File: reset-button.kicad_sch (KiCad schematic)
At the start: 3 parts, among them SW1 SW_MEC_5E

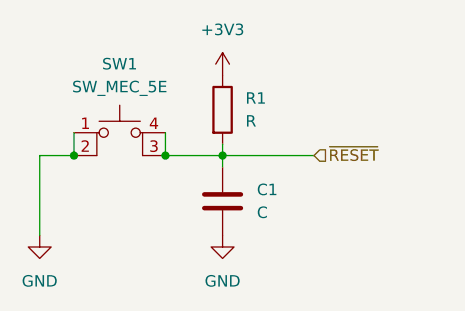
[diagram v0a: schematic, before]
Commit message: Adding symbols information
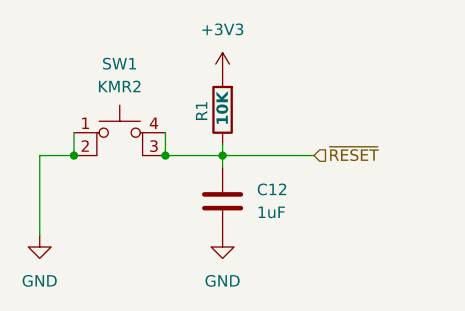
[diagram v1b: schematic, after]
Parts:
- C12: renamed from C1; value C -> 1uF; footprint (none) -> Capacitor_SMD:C_0603_1608Metric; Mfr (none) -> YAGEO; Mfr P/N (none) -> CC0603KRX7R7BB105; Supplier_1 (none) -> Digikey; Supplier_1 P/N (none) -> 0.10; Supplier_1 Unit Price (none) -> 0.03080
- R1: value R -> 10K; footprint (none) -> Resistor_SMD:R_0603_1608Metric; Mfr (none) -> Stackpole Electronics Inc; Mfr P/N (none) -> RNCP0603FTD10K0; Supplier_1 (none) -> Digikey; Supplier_1 P/N (none) -> RNCP0603FTD10K0CT-ND; Supplier_1 Price @ Qty (none) -> 0.0170; Supplier_1 Unit Price (none) -> 0.10
- SW1: value SW_MEC_5E -> KMR2; footprint (none) -> Button_Switch_SMD:SW_Push_1P1T_NO_CK_KMR2; Mfr (none) -> C&K; Mfr P/N (none) -> KM241NG ULC LFS; Supplier_1 (none) -> Digikey; Supplier_1 P/N (none) -> CKN10285CT-ND; Supplier_1 Price @ Qty (none) -> 0.72030; Supplier_1 Unit Price (none) -> 0.92
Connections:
- net +3V3: now also R1.2; no longer R1.1
- net ~{RESET}: now also R1.1; no longer R1.2
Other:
- company: (none) -> catbranchman
- title: (none) -> Reset Button

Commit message: Starting layout
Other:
- moved on the sheet: C12, R1
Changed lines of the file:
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@@
 	)
 	(junction
-		(at 153.67 97.79)
+		(at 156.21 97.79)
 		(diameter 0)
 		(color 0 0 0 0)
 	)
 	(junction
-		(at 137.16 97.79)
+		(at 135.89 97.79)
 		(diameter 0)
 		(color 0 0 0 0)
 	)
 	(junction
-		(at 147.32 97.79)
+		(at 148.59 97.79)
 		(diameter 0)
 		(color 0 0 0 0)
@@
 	(wire
 		(pts
-			(xy 153.67 97.79) (xy 153.67 99.06)
-		)
-		(stroke
-			(width 0)
-			(type default)
-		)
-	)
-	(wire
-		(pts
-			(xy 137.16 95.25) (xy 137.16 97.79)
+			(xy 156.21 97.79) (xy 156.21 99.06)
+		)
+		(stroke
+			(width 0)
+			(type default)
+		)
+	)
+	(wire
+		(pts
+			(xy 135.89 97.79) (xy 137.16 97.79)
+		)
+		(stroke
+			(width 0)
+			(type default)
+		)
+	)
+	(wire
+		(pts
+			(xy 133.35 97.79) (xy 135.89 97.79)
 		)
 		(stroke
@@
 	(wire
 		(pts
-			(xy 147.32 95.25) (xy 147.32 97.79)
-		)
-		(stroke
-			(width 0)
-			(type default)
-		)
-	)
-	(wire
-		(pts
-			(xy 147.32 97.79) (xy 153.67 97.79)
-		)
-		(stroke
-			(width 0)
-			(type default)
-		)
-	)
-	(wire
-		(pts
-			(xy 153.67 97.79) (xy 163.83 97.79)
-		)
-		(stroke
-			(width 0)
-			(type default)
-		)
-	)
-	(wire
-		(pts
-			(xy 133.35 97.79) (xy 137.16 97.79)
-		)
-		(stroke
-			(width 0)
-			(type default)
-		)
-	)
-	(wire
-		(pts
-			(xy 153.67 97.79) (xy 153.67 96.52)
+			(xy 148.59 95.25) (xy 148.59 97.79)
+		)
+		(stroke
+			(width 0)
+			(type default)
+		)
+	)
+	(wire
+		(pts
+			(xy 135.89 95.25) (xy 135.89 97.79)
+		)
+		(stroke
+			(width 0)
+			(type default)
+		)
+	)
+	(wire
+		(pts
+			(xy 156.21 97.79) (xy 166.37 97.79)
+		)
+		(stroke
+			(width 0)
+			(type default)
+		)
+	)
+	(wire
+		(pts
+			(xy 147.32 97.79) (xy 148.59 97.79)
+		)
+		(stroke
+			(width 0)
+			(type default)
+		)
+	)
+	(wire
+		(pts
+			(xy 148.59 95.25) (xy 147.32 95.25)
+		)
+		(stroke
+			(width 0)
+			(type default)
+		)
+	)
+	(wire
+		(pts
+			(xy 156.21 97.79) (xy 156.21 96.52)
+		)
+		(stroke
+			(width 0)
+			(type default)
+		)
+	)
+	(wire
+		(pts
+			(xy 148.59 97.79) (xy 156.21 97.79)
+		)
+		(stroke
+			(width 0)
+			(type default)
+		)
+	)
+	(wire
+		(pts
+			(xy 137.16 95.25) (xy 135.89 95.25)
 		)
 		(stroke
@@
 	(hierarchical_label "~{RESET}"
 		(shape input)
-		(at 163.83 97.79 0)
+		(at 166.37 97.79 0)
 		(fields_autoplaced yes)
 		(effects
@@
 	(symbol
 		(lib_id "Device:C")
-		(at 153.67 102.87 0)
+		(at 156.21 102.87 0)
 		(unit 1)
 		(exclude_from_sim no)
@@
 		(fields_autoplaced yes)
 		(property "Reference" "C12"
-			(at 157.48 101.5999 0)
+			(at 160.02 101.5999 0)
 			(effects
 				(font
@@
 		)
 		(property "Value" "1uF"
-			(at 157.48 104.1399 0)
+			(at 160.02 104.1399 0)
 			(effects
 				(font
@@
 		)
 		(property "Footprint" "Capacitor_SMD:C_0603_1608Metric"
-			(at 154.6352 106.68 0)
+			(at 157.1752 106.68 0)
 			(effects
 				(font
@@
 		)
 		(property "Datasheet" "https://www.yageo.com/upload/media/product/productsearch/datasheet/mlcc/UPY-GPHC_X7R_6"
-			(at 153.67 102.87 0)
+			(at 156.21 102.87 0)
 			(effects
 				(font
@@
 		)
 		(property "Description" "1 uF 10% 16V Ceramic Capacitor X7R 0603 (1608 Metric)"
-			(at 153.67 102.87 0)
+			(at 156.21 102.87 0)
 			(effects
 				(font
@@
 		)
 		(property "Mfr" "YAGEO"
-			(at 153.67 102.87 0)
+			(at 156.21 102.87 0)
 			(effects
 				(font
@@
 		)
 		(property "Mfr P/N" "CC0603KRX7R7BB105"
-			(at 153.67 102.87 0)
+			(at 156.21 102.87 0)
 			(effects
 				(font
@@
 		)
 		(property "Supplier_1" "Digikey"
-			(at 153.67 102.87 0)
+			(at 156.21 102.87 0)
 			(effects
 				(font
@@
 		)
 		(property "Supplier_1 P/N" "0.10"
-			(at 153.67 102.87 0)
+			(at 156.21 102.87 0)
 			(effects
 				(font
@@
 		)
 		(property "Supplier_1 Unit Price" "0.03080"
-			(at 153.67 102.87 0)
+			(at 156.21 102.87 0)
 			(effects
 				(font
@@
 		)
 		(property "Supplier_1 Price @ Qty" ""
-			(at 153.67 102.87 0)
+			(at 156.21 102.87 0)
 			(effects
 				(font
@@
 		)
 		(property "Supplier_2" ""
-			(at 153.67 102.87 0)
+			(at 156.21 102.87 0)
 			(effects
 				(font
@@
 		)
 		(property "Supplier_2 P/N" ""
-			(at 153.67 102.87 0)
+			(at 156.21 102.87 0)
 			(effects
 				(font
@@
 		)
 		(property "Supplier_2 Unit Price" ""
-			(at 153.67 102.87 0)
+			(at 156.21 102.87 0)
 			(effects
 				(font
@@
 		)
 		(property "Supplier_2 Price @ Qty" ""
-			(at 153.67 102.87 0)
+			(at 156.21 102.87 0)
 			(effects
 				(font
@@
 	(symbol
 		(lib_id "Device:R")
-		(at 153.67 92.71 180)
+		(at 156.21 92.71 180)
 		(unit 1)
 		(exclude_from_sim no)
@@
 		(dnp no)
 		(property "Reference" "R1"
-			(at 151.384 91.694 90)
+			(at 153.924 91.694 90)
 			(effects
 				(font
@@
 		)
 		(property "Value" "10K"
-			(at 153.67 90.678 90)
+			(at 156.21 90.678 90)
 			(effects
 				(font
@@
 		)
 		(property "Footprint" "Resistor_SMD:R_0603_1608Metric"
-			(at 155.448 92.71 90)
+			(at 157.988 92.71 90)
 			(effects
 				(font
@@
 		)
 		(property "Datasheet" "https://www.seielect.com/catalog/sei-rncp.pdf"
-			(at 153.67 92.71 0)
+			(at 156.21 92.71 0)
 			(effects
 				(font
@@
 		)
 		(property "Description" "10 kOhms 1% 0.125W, 1/8W Chip Resistor 0603 (1608 Metric) Anti-Sulfur Thin Film"
-			(at 153.67 92.71 0)
+			(at 156.21 92.71 0)
 			(effects
 				(font
@@
 		)
 		(property "Mfr" "Stackpole Electronics Inc"
-			(at 153.67 92.71 0)
+			(at 156.21 92.71 0)
 			(effects
 				(font
@@
 		)
 		(property "Mfr P/N" "RNCP0603FTD10K0"
-			(at 153.67 92.71 0)
+			(at 156.21 92.71 0)
 			(effects
 				(font
@@
 		)
 		(property "Supplier_1" "Digikey"
-			(at 153.67 92.71 0)
+			(at 156.21 92.71 0)
 			(effects
 				(font
@@
 		)
 		(property "Supplier_1 P/N" "RNCP0603FTD10K0CT-ND"
-			(at 153.67 92.71 0)
+			(at 156.21 92.71 0)
 			(effects
 				(font
@@
 		)
 		(property "Supplier_1 Unit Price" "0.10"
-			(at 153.67 92.71 0)
+			(at 156.21 92.71 0)
 			(effects
 				(font
@@
 		)
 		(property "Supplier_1 Price @ Qty" "0.0170"
-			(at 153.67 92.71 0)
+			(at 156.21 92.71 0)
 			(effects
 				(font
@@
 		)
 		(property "Supplier_2" ""
-			(at 153.67 92.71 0)
+			(at 156.21 92.71 0)
 			(effects
 				(font
@@
 		)
 		(property "Supplier_2 P/N" ""
-			(at 153.67 92.71 0)
+			(at 156.21 92.71 0)
 			(effects
 				(font
@@
 		)
 		(property "Supplier_2 Unit Price" ""
-			(at 153.67 92.71 0)
+			(at 156.21 92.71 0)
 			(effects
 				(font
@@
 		)
 		(property "Supplier_2 Price @ Qty" ""
-			(at 153.67 92.71 0)
+			(at 156.21 92.71 0)
 			(effects
 				(font
@@
 	(symbol
 		(lib_id "power:+3V3")
-		(at 153.67 88.9 0)
+		(at 156.21 88.9 0)
 		(unit 1)
 		(exclude_from_sim no)
@@
 		(fields_autoplaced yes)
 		(property "Reference" "#PWR03"
-			(at 153.67 92.71 0)
+			(at 156.21 92.71 0)
 			(effects
 				(font
@@
 		)
 		(property "Value" "+3V3"
-			(at 153.67 83.82 0)
+			(at 156.21 83.82 0)
 			(effects
 				(font
@@
 		)
 		(property "Footprint" ""
-			(at 153.67 88.9 0)
+			(at 156.21 88.9 0)
 			(effects
 				(font
@@
 		)
 		(property "Datasheet" ""
-			(at 153.67 88.9 0)
+			(at 156.21 88.9 0)
 			(effects
 				(font
@@
 		)
 		(property "Description" "Power symbol creates a global label with name \"+3V3\""
-			(at 153.67 88.9 0)
+			(at 156.21 88.9 0)
 			(effects
 				(font
@@
 	(symbol
 		(lib_id "power:GND")
-		(at 153.67 106.68 0)
+		(at 156.21 106.68 0)
 		(unit 1)
 		(exclude_from_sim no)
@@
 		(fields_autoplaced yes)
 		(property "Reference" "#PWR02"
-			(at 153.67 113.03 0)
+			(at 156.21 113.03 0)
 			(effects
 				(font
@@
 		)
 		(property "Value" "GND"
-			(at 153.67 111.76 0)
+			(at 156.21 111.76 0)
 			(effects
 				(font
@@
 		)
 		(property "Footprint" ""
-			(at 153.67 106.68 0)
+			(at 156.21 106.68 0)
 			(effects
 				(font
@@
 		)
 		(property "Datasheet" ""
-			(at 153.67 106.68 0)
+			(at 156.21 106.68 0)
 			(effects
 				(font
@@
 		)
 		(property "Description" "Power symbol creates a global label with name \"GND\" , ground"
-			(at 153.67 106.68 0)
-			(effects
-				(font
+			(at 156.21 106.68 0)
+			(effects
+				(font

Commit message: Working on layout
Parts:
- removed SW1: KMR2, Button_Switch_SMD:SW_Push_1P1T_NO_CK_KMR2, symbol Switch:SW_MEC_5E
- added SW1: KMR2, Button_Switch_SMD:SW_Push_1P1T_NO_CK_KMR2, symbol Switch:SW_Push
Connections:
- net GND: now also SW1.1
- net ~{RESET}: now also SW1.2
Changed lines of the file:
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@@
-		(color 0 0 0 0)
-	)
-	(junction
-		(at 135.89 97.79)
-		(diameter 0)
-		(color 0 0 0 0)
-	)
-	(junction
-		(at 148.59 97.79)
-		(diameter 0)
 		(color 0 0 0 0)
 	)
@@
 	(wire
 		(pts
-			(xy 135.89 97.79) (xy 137.16 97.79)
+			(xy 133.35 97.79) (xy 137.16 97.79)
 		)
 		(stroke
@@
 	(wire
 		(pts
-			(xy 133.35 97.79) (xy 135.89 97.79)
+			(xy 133.35 106.68) (xy 133.35 97.79)
 		)
 		(stroke
@@
 	(wire
 		(pts
-			(xy 133.35 106.68) (xy 133.35 97.79)
+			(xy 156.21 97.79) (xy 166.37 97.79)
 		)
 		(stroke
@@
 	(wire
 		(pts
-			(xy 148.59 95.25) (xy 148.59 97.79)
+			(xy 147.32 97.79) (xy 156.21 97.79)
 		)
 		(stroke
@@
 	(wire
 		(pts
-			(xy 135.89 95.25) (xy 135.89 97.79)
-		)
-		(stroke
-			(width 0)
-			(type default)
-		)
-	)
-	(wire
-		(pts
-			(xy 156.21 97.79) (xy 166.37 97.79)
-		)
-		(stroke
-			(width 0)
-			(type default)
-		)
-	)
-	(wire
-		(pts
-			(xy 147.32 97.79) (xy 148.59 97.79)
-		)
-		(stroke
-			(width 0)
-			(type default)
-		)
-	)
-	(wire
-		(pts
-			(xy 148.59 95.25) (xy 147.32 95.25)
-		)
-		(stroke
-			(width 0)
-			(type default)
-		)
-	)
-	(wire
-		(pts
 			(xy 156.21 97.79) (xy 156.21 96.52)
-		)
-		(stroke
-			(width 0)
-			(type default)
-		)
-	)
-	(wire
-		(pts
-			(xy 148.59 97.79) (xy 156.21 97.79)
-		)
-		(stroke
-			(width 0)
-			(type default)
-		)
-	)
-	(wire
-		(pts
-			(xy 137.16 95.25) (xy 135.89 95.25)
 		)
 		(stroke
@@
 	)
 	(symbol
-		(lib_id "Switch:SW_MEC_5E")
-		(at 142.24 97.79 0)
-		(unit 1)
-		(exclude_from_sim no)
-		(in_bom yes)
-		(on_board yes)
-		(dnp no)
-		(fields_autoplaced yes)
-		(property "Reference" "SW1"
-			(at 142.24 87.63 0)
-			(effects
-				(font
-					(size 1.27 1.27)
-				)
-			)
-		)
-		(property "Value" "KMR2"
-			(at 142.24 90.17 0)
-			(effects
-				(font
-					(size 1.27 1.27)
-				)
-			)
-		)
-		(property "Footprint" "Button_Switch_SMD:SW_Push_1P1T_NO_CK_KMR2"
-			(at 142.24 90.17 0)
-			(effects
-				(font
-					(size 1.27 1.27)
-				)
-				(hide yes)
-			)
-		)
-		(property "Datasheet" "https://www.ckswitches.com/media/1479/kmr2.pdf"
-			(at 142.24 90.17 0)
-			(effects
-				(font
-					(size 1.27 1.27)
-				)
-				(hide yes)
-			)
-		)
-		(property "Description" "Tactile Switch SPST-NO Top Actuated Surface Mount 0.05A @ 32 VDC 400gf"
-			(at 142.24 97.79 0)
-			(effects
-				(font
-					(size 1.27 1.27)
-				)
-				(hide yes)
-			)
-		)
-		(property "Mfr" "C&K"
-			(at 142.24 97.79 0)
-			(effects
-				(font
-					(size 1.27 1.27)
-				)
-				(hide yes)
-			)
-		)
-		(property "Mfr P/N" "KM241NG ULC LFS"
-			(at 142.24 97.79 0)
-			(effects
-				(font
-					(size 1.27 1.27)
-				)
-				(hide yes)
-			)
-		)
-		(property "Supplier_1" "Digikey"
-			(at 142.24 97.79 0)
-			(effects
-				(font
-					(size 1.27 1.27)
-				)
-				(hide yes)
-			)
-		)
-		(property "Supplier_1 P/N" "CKN10285CT-ND"
-			(at 142.24 97.79 0)
-			(effects
-				(font
-					(size 1.27 1.27)
-				)
-				(hide yes)
-			)
-		)
-		(property "Supplier_1 Unit Price" "0.92"
-			(at 142.24 97.79 0)
-			(effects
-				(font
-					(size 1.27 1.27)
-				)
-				(hide yes)
-			)
-		)
-		(property "Supplier_1 Price @ Qty" "0.72030"
-			(at 142.24 97.79 0)
-			(effects
-				(font
-					(size 1.27 1.27)
-				)
-				(hide yes)
-			)
-		)
-		(property "Supplier_2" ""
-			(at 142.24 97.79 0)
-			(effects
-				(font
-					(size 1.27 1.27)
-				)
-				(hide yes)
-			)
-		)
-		(property "Supplier_2 P/N" ""
-			(at 142.24 97.79 0)
-			(effects
-				(font
-					(size 1.27 1.27)
-				)
-				(hide yes)
-			)
-		)
-		(property "Supplier_2 Unit Price" ""
-			(at 142.24 97.79 0)
-			(effects
-				(font
-					(size 1.27 1.27)
-				)
-				(hide yes)
-			)
-		)
-		(property "Supplier_2 Price @ Qty" ""
-			(at 142.24 97.79 0)
-			(effects
-				(font
-					(size 1.27 1.27)
-				)
-				(hide yes)
-			)
-		)
-		(pin "2"
-		)
-		(pin "3"
-		)
-		(pin "4"
-		)
-		(pin "1"
-		)
-		(instances
-			(project "roamer"
-				(path "/1c59de6a-87fe-4223-8898-4b0383164a31/c211aea2-d57b-4e05-ad36-57285d8bb57b"
-					(reference "SW1")
-					(unit 1)
-				)
-			)
-		)
-	)
-	(symbol
 		(lib_id "power:+3V3")
 		(at 156.21 88.9 0)
@@
 					(unit 1)
 				)
+			)
+		)
+	)
+	(symbol
+		(lib_id "Switch:SW_Push")
+		(at 142.24 97.79 0)
+		(unit 1)
+		(exclude_from_sim no)
+		(in_bom yes)
+		(on_board yes)
+		(dnp no)
+		(fields_autoplaced yes)
+		(property "Reference" "SW1"
+			(at 142.24 90.17 0)
+			(effects
+				(font
+					(size 1.27 1.27)
+				)
+			)
+		)
+		(property "Value" "KMR2"
+			(at 142.24 92.71 0)
+			(effects
+				(font
+					(size 1.27 1.27)
+				)
+			)
+		)
+		(property "Footprint" "Button_Switch_SMD:SW_Push_1P1T_NO_CK_KMR2"
+			(at 142.24 92.71 0)
+			(effects
+				(font
+					(size 1.27 1.27)
+				)
+				(hide yes)
+			)
+		)
+		(property "Datasheet" "https://www.ckswitches.com/media/1479/kmr2.pdf"
+			(at 142.24 92.71 0)
+			(effects
+				(font
+					(size 1.27 1.27)
+				)
+				(hide yes)
+			)
+		)
+		(property "Description" "Push button switch, generic, two pins"
+			(at 142.24 97.79 0)
+			(effects
+				(font
+					(size 1.27 1.27)
+				)
+				(hide yes)
+			)
+		)
+		(property "Mfr" "C&K"
+			(at 142.24 97.79 0)
+			(effects
+				(font
+					(size 1.27 1.27)
+				)
+				(hide yes)
+			)
+		)
+		(property "Mfr P/N" "KM241NG ULC LFS"
+			(at 142.24 97.79 0)
+			(effects
+				(font
+					(size 1.27 1.27)
+				)
+				(hide yes)
+			)
+		)
+		(property "Supplier_1" "Digikey"
+			(at 142.24 97.79 0)
+			(effects
+				(font
+					(size 1.27 1.27)
+				)
+				(hide yes)
+			)
+		)
+		(property "Supplier_1 P/N" "CKN10285CT-ND"
+			(at 142.24 97.79 0)
+			(effects
+				(font
+					(size 1.27 1.27)
+				)
+				(hide yes)
+			)
+		)
+		(property "Supplier_1 Unit Price" "$0.92"
+			(at 142.24 97.79 0)
+			(effects
+				(font
+					(size 1.27 1.27)
+				)
+				(hide yes)
+			)
+		)
+		(property "Supplier_1 Price @ Qty" "0.72030"
+			(at 142.24 97.79 0)
+			(effects
+				(font
+					(size 1.27 1.27)
+				)
+				(hide yes)
+			)
+		)
+		(property "Supplier_2" ""
+			(at 142.24 97.79 0)
+			(effects
+				(font
+					(size 1.27 1.27)
+				)
+				(hide yes)
+			)
+		)
+		(property "Supplier_2 P/N" ""
+			(at 142.24 97.79 0)
+			(effects
+				(font
+					(size 1.27 1.27)
+				)
+				(hide yes)
+			)
+		)
+		(property "Supplier_2 Unit Price" ""
+			(at 142.24 97.79 0)
+			(effects
+				(font
+					(size 1.27 1.27)
+				)
+				(hide yes)
+			)
+		)
+		(property "Supplier_2 Price @ Qty" ""
+			(at 142.24 97.79 0)
+			(effects
+				(font
+					(size 1.27 1.27)
+				)
+				(hide yes)
+			)
+		)
+		(pin "2"
+		)
+		(pin "1"
+		)
+		(instances
+			(project ""
+				(path "/1c59de6a-87fe-4223-8898-4b0383164a31/c211aea2-d57b-4e05-ad36-57285d8bb57b"
+					(reference "SW1")
+					(unit 1)
+				)

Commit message: Creating fab package
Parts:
- SW1: Supplier_1 Unit Price $0.92 -> 0.92
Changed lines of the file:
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@@
 			)
 		)
-		(property "Supplier_1 Unit Price" "$0.92"
+		(property "Supplier_1 Unit Price" "0.92"
 			(at 142.24 97.79 0)
 			(effects
